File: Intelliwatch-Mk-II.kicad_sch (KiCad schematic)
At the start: 55 parts, among them J1 USB_C_Receptacle_USB2.0_16P, J2 CONN LCD 1.8 TFT SPI, J3 Conn 7S-4D HW-069 I2C, J4 Flashlight Terminals, Q1 NTR2101P, Q2 NDS331N, SW1 EN Switch, SW2 PROG Swtich, SW3 Cherry MX Keyswitch, SW4 Cherry MX Keyswitch, SW5 Cherry MX Keyswitch, SW6 Cherry MX Keyswitch, U1 LM7805, U2 CH340C, U3 SN74HC02N, U4 LM1117T-3.3, U5 74AHC1G04GW_125, U6 74AHC1G04GW_125, U7 ESP32-WROOM-32UE, U8 QMC5883L

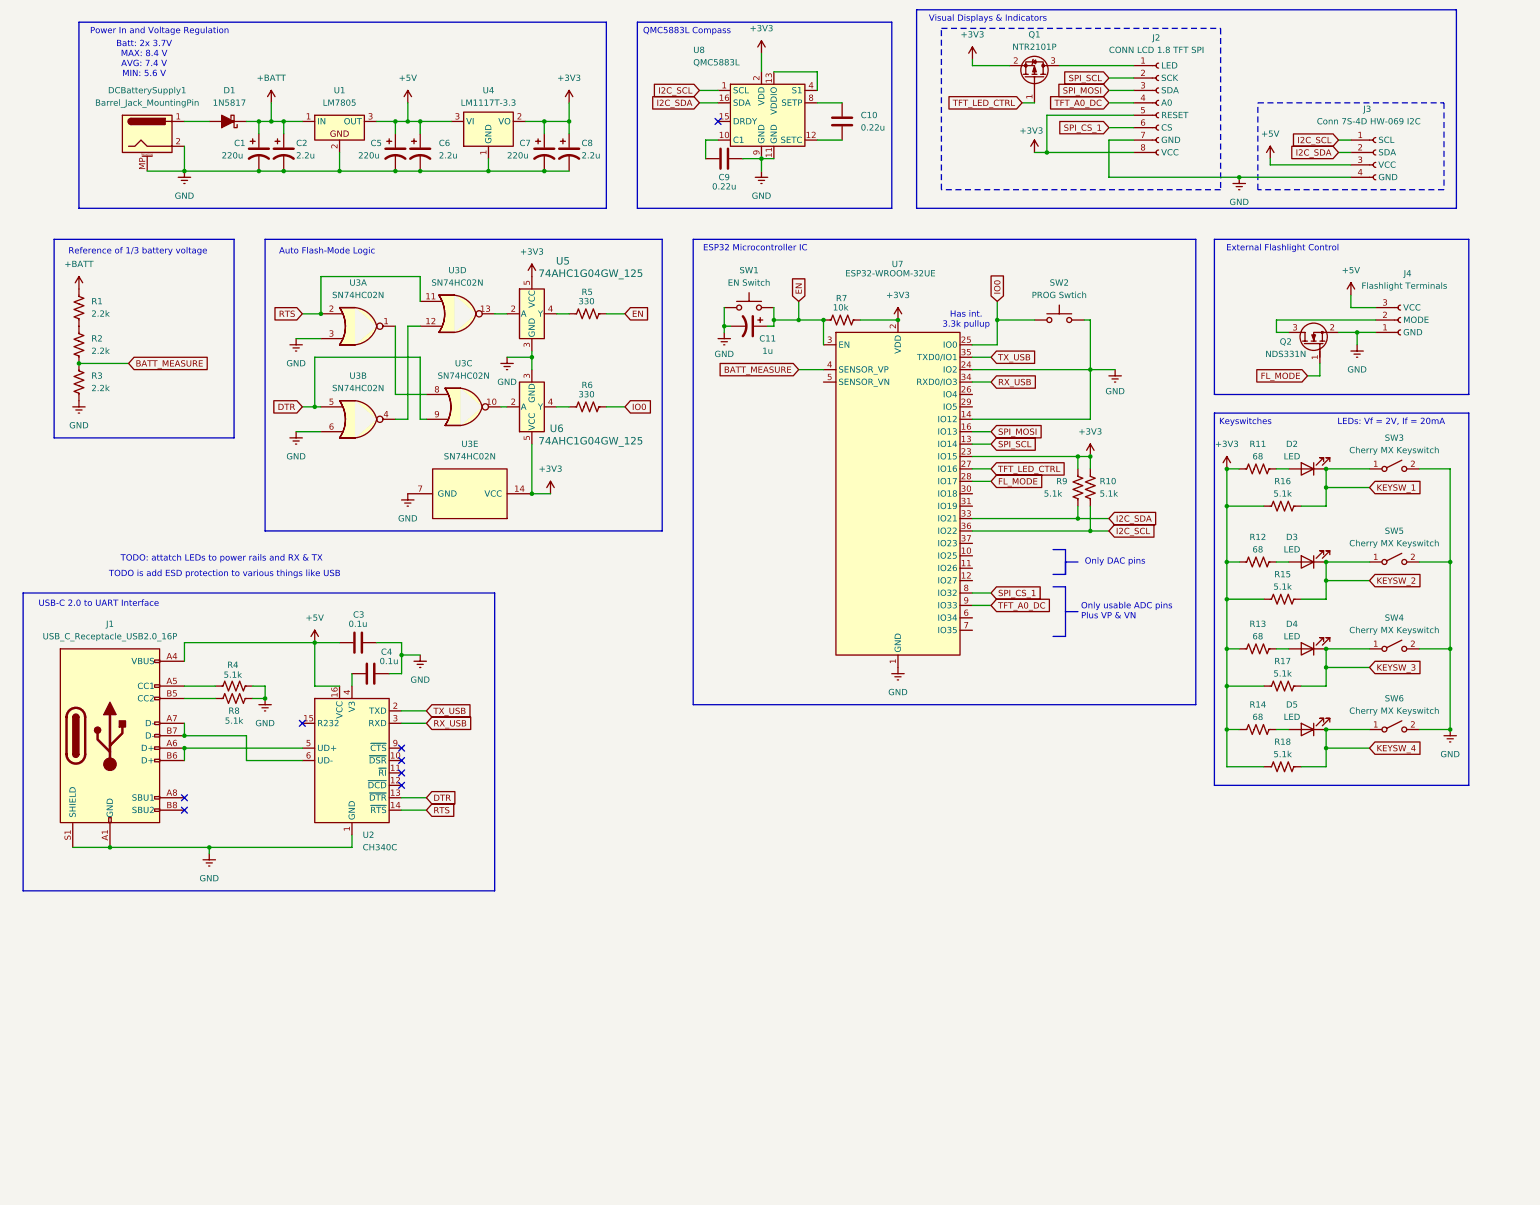
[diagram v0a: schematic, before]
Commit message: ADDED current draw for each component. ADDED flashlight. WIP TODO is sort out whether or not to re-use VSPI MOSI and SCL pins with both LCD and SD card.
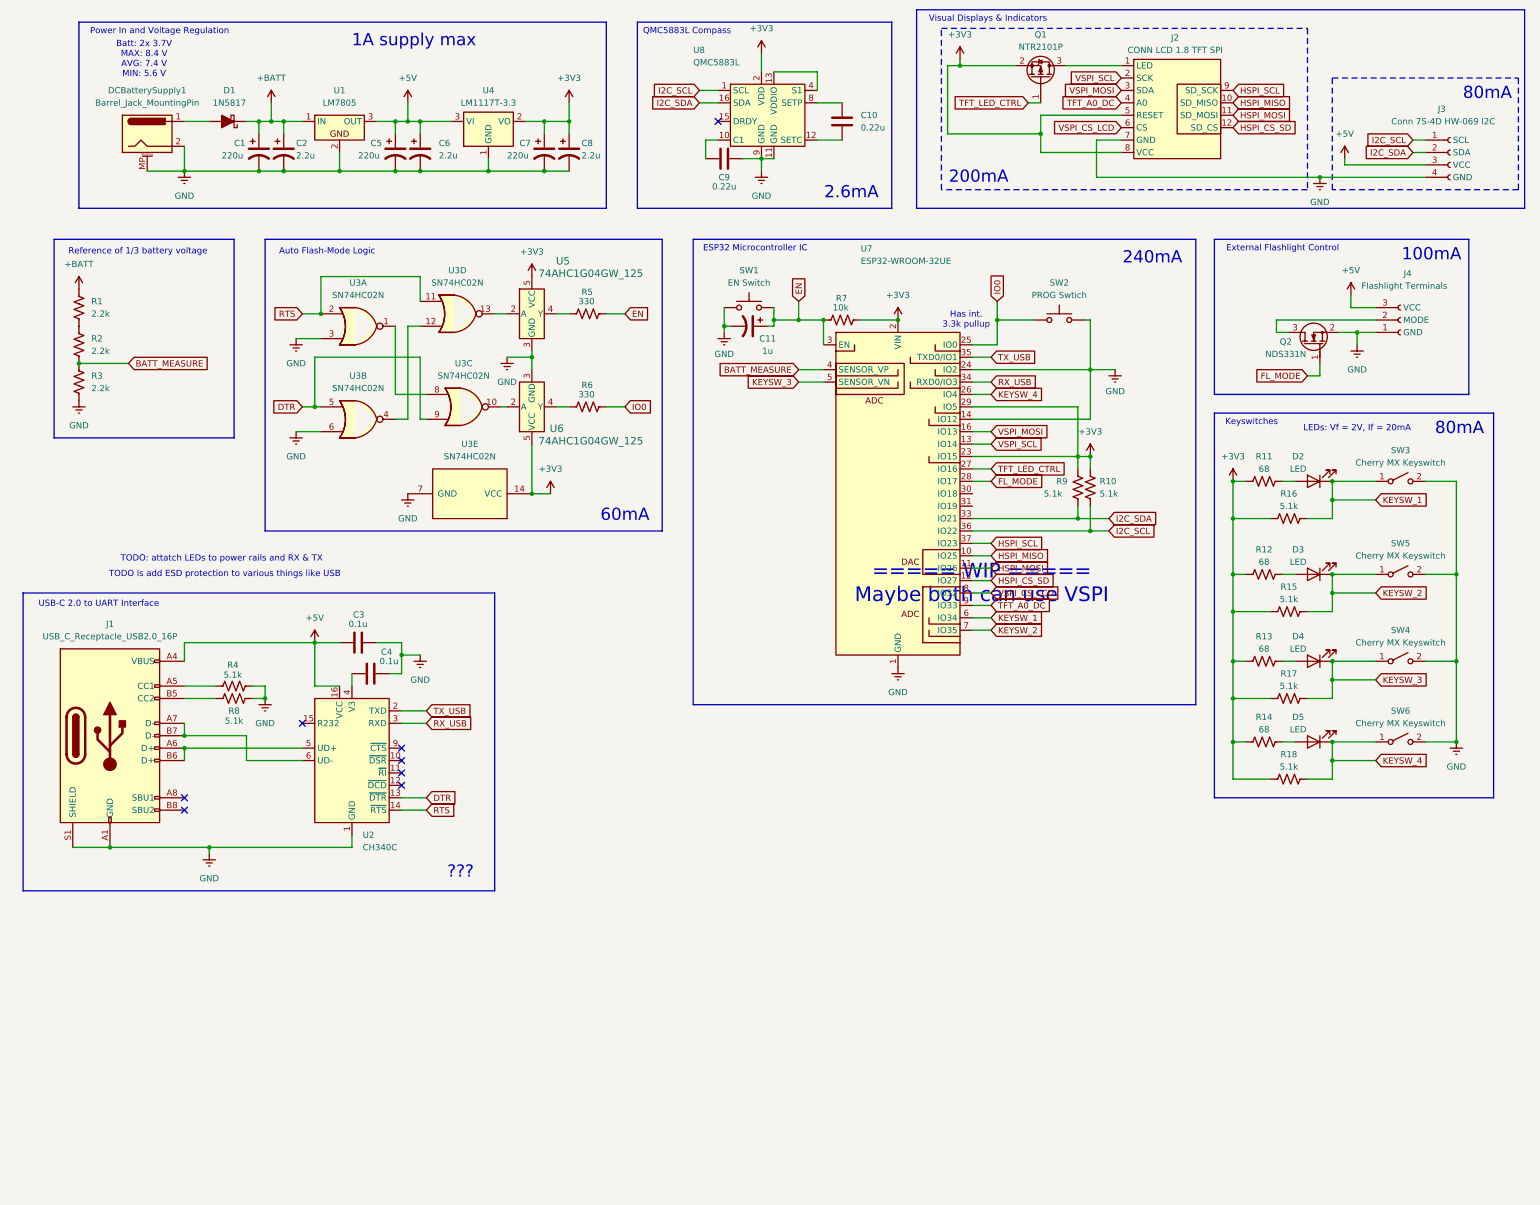
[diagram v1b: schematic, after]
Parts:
- removed U7: ESP32-WROOM-32UE, RF_Module:ESP32-WROOM-32UE, symbol RF_Module:ESP32-WROOM-32UE
- added U7: ESP32-WROOM-32UE, RF_Module:ESP32-WROOM-32UE, symbol ZCustomSymbols:ESP32-WROOM-32UE
- U2: footprint Package_SO:SOIC-16_3.9x9.9mm_P1.27mm -> PCM_Package_SO_AKL:SOP-16_4.55x10.3mm_P1.27mm
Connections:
- net +3V3: now also U7.2 (VIN), U7.23 (IO15), U7.29 (IO5)
- net BATT_MEASURE: now also U7.4 (SENSOR_VP)
- net EN: now also U7.3 (EN)
- net FL_MODE: now also U7.28 (IO17)
- net GND: now also U7.1 (GND), U7.14 (IO12), U7.15 (GND), U7.24 (IO2), U7.38 (GND), U7.39 (GND)
- net I2C_SCL: now also U7.36 (IO22)
- net I2C_SDA: now also U7.33 (IO21)
- net IO0: now also U7.25 (IO0)
- net KEYSW_1: now also U7.6 (IO34)
- net KEYSW_2: now also U7.7 (IO35)
- net KEYSW_3: now also U7.5 (SENSOR_VN)
- net KEYSW_4: now also U7.26 (IO4)
- net RX_USB: now also U7.34 (RXD0/IO3)
- net TFT_A0_DC: now also U7.9 (IO33)
- net TFT_LED_CTRL: now also U7.27 (IO16)
- net TX_USB: now also U7.35 (TXD0/IO1)
- net SPI_CS_1 renamed VSPI_CS_LCD
- net VSPI_CS_LCD: now also U7.8 (IO32)
- net SPI_MOSI renamed VSPI_MOSI
- net VSPI_MOSI: now also U7.16 (IO13)
- net SPI_SCL renamed VSPI_SCL
- net VSPI_SCL: now also U7.13 (IO14)
- new net HSPI_CS_SD: J2.12 (SD_CS), U7.12 (IO27)
- new net HSPI_MISO: J2.10 (SD_MISO), U7.10 (IO25)
- new net HSPI_MOSI: J2.11 (SD_MOSI), U7.11 (IO26)
- new net HSPI_SCL: J2.9 (SD_SCK), U7.37 (IO23)
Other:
- note added: "100mA"
- note added: "1A supply max"
- note added: "2.6mA"
- note added: "200mA"
- note added: "240mA"
- note added: "60mA"
- note added: "80mA"
- note added: "===== WIP ===== Maybe both can use VSPI"
- note added: "???"
- note removed: "Only DAC pins"
- note removed: "Only usable ADC pins Plus VP & VN"
- moved on the sheet: D2, D3, D4, D5, J3, Q1, R11, R12, R13, R14, R15, R16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

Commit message: ADDED ADC for voltmeter/o-scope (NO res-measuring in this one). WIP TODO is determine whether or not SD and LCD will share SPI bus. TODO change voltage regulators to IC-controller buck converters.
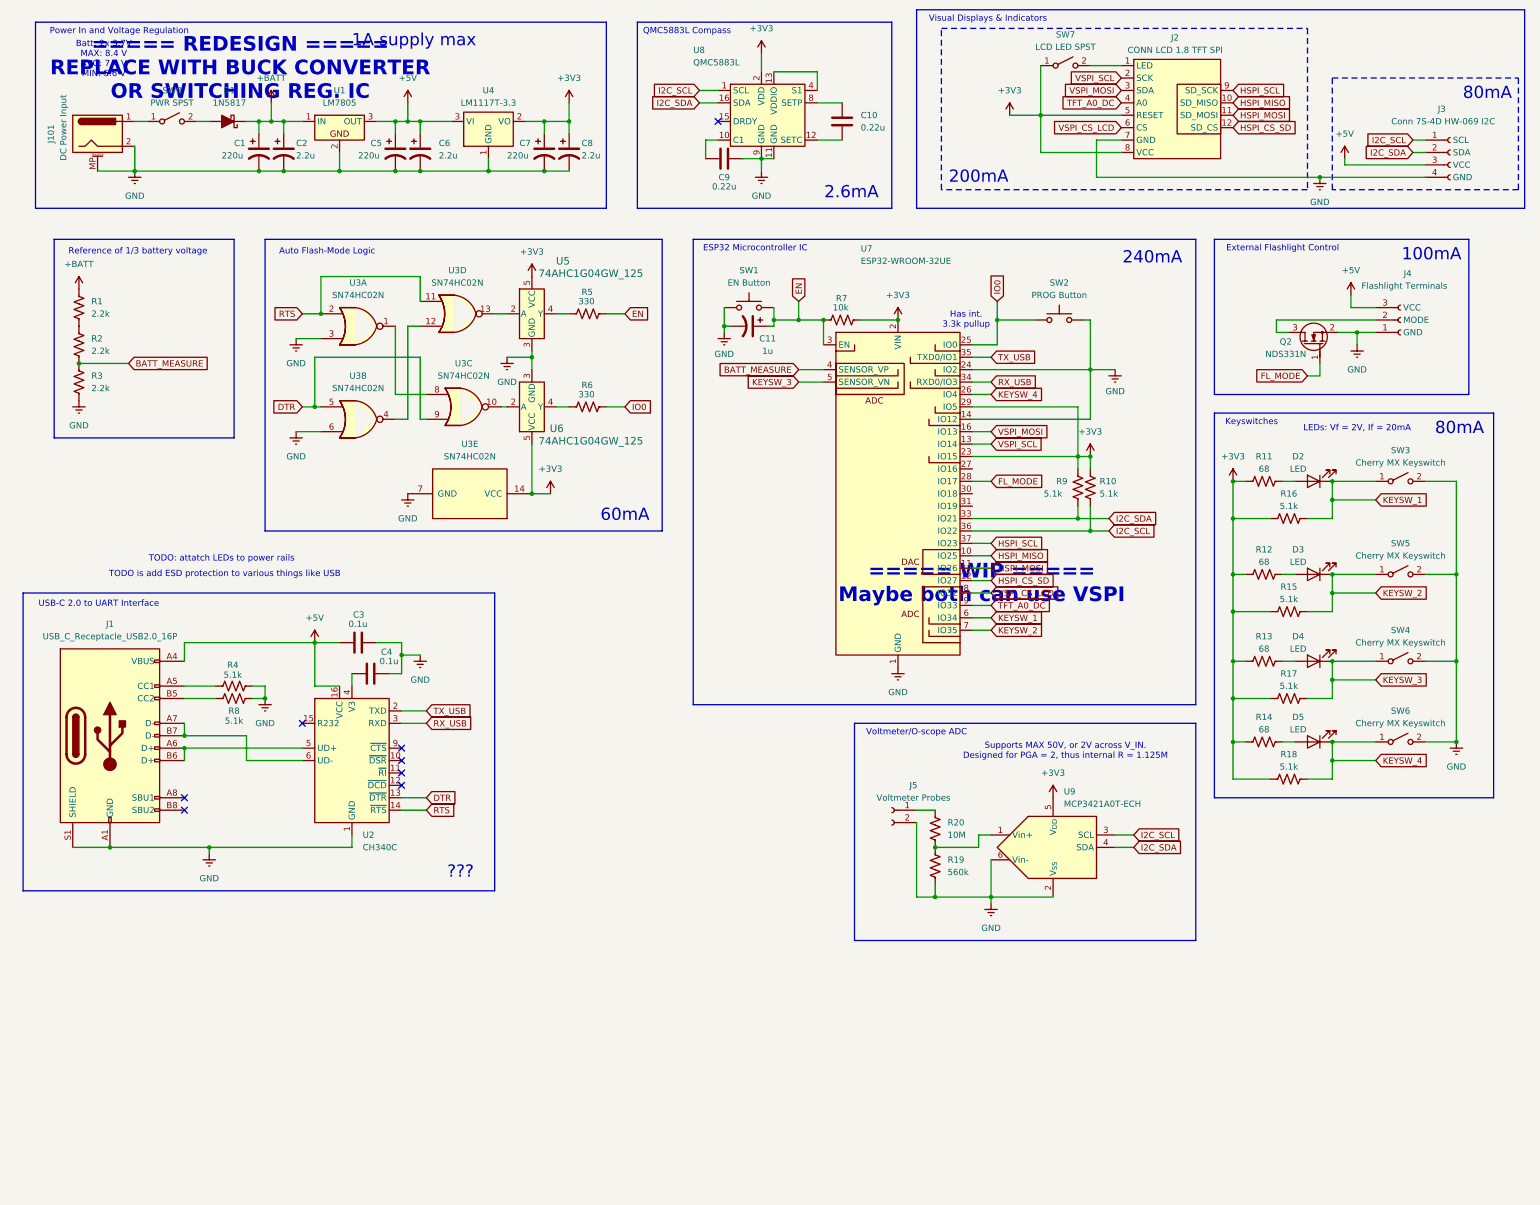
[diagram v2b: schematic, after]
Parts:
- removed Q1: NTR2101P, Package_TO_SOT_SMD:SOT-23, symbol Transistor_FET:NTR2101P
- added J5: Voltmeter Probes, symbol Connector:Conn_01x02_Socket
- added R19: 560k, symbol Device:R_US
- added R20: 10M, symbol Device:R_US
- added SW7: LCD LED SPST, symbol Switch:SW_SPST
- added SW8: PWR SPST, symbol Switch:SW_SPST
- added U9: MCP3421A0T-ECH, PCM_Package_TO_SOT_SMD_AKL:SOT-23-6, symbol Analog_ADC:MCP3421A0T-ECH
- J101: renamed from DCBatterySupply1; value Barrel_Jack_MountingPin -> DC Power Input
- SW1: value EN Switch -> EN Button
- SW2: value PROG Swtich -> PROG Button
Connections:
- net +3V3: now also SW7.1 (A), U9.5 (V_{DD})
- net GND: now also J5.2 (Pin_2), R19.2, U9.2 (V_{SS}), U9.6 (Vin-)
- net I2C_SCL: now also U9.3 (SCL)
- net I2C_SDA: now also U9.4 (SDA)
- net at D1.2 (A): now also SW8.2 (B); no longer J101.1
- net at J2.1 (LED): now also SW7.2 (B)
- net TFT_LED_CTRL: no longer names the net of U7.27 (IO16)
- new net: R19.1, R20.1, U9.1 (Vin+)
- new net: J5.1 (Pin_1), R20.2
- new net: J101.1, SW8.1 (A)
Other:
- note added: "===== REDESIGN ===== REPLACE WITH BUCK CONVERTER OR SWITCHING REG. IC"
- note added: "Supports MAX 50V, or 2V across V_IN. Designed for PGA = 2, thus internal R = 1.125M"
- note added: "TODO: attatch LEDs to power rails"
- note added: "Voltmeter/O-scope ADC"
- note removed: "TODO: attatch LEDs to power rails and RX & TX"
- moved on the sheet: J101

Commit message: ADDED 3.3V step-down switching regulator (buck converter). TODO delete old power setup, but keep 5V regulator because that has low maximum short-term current draw so it's fine.
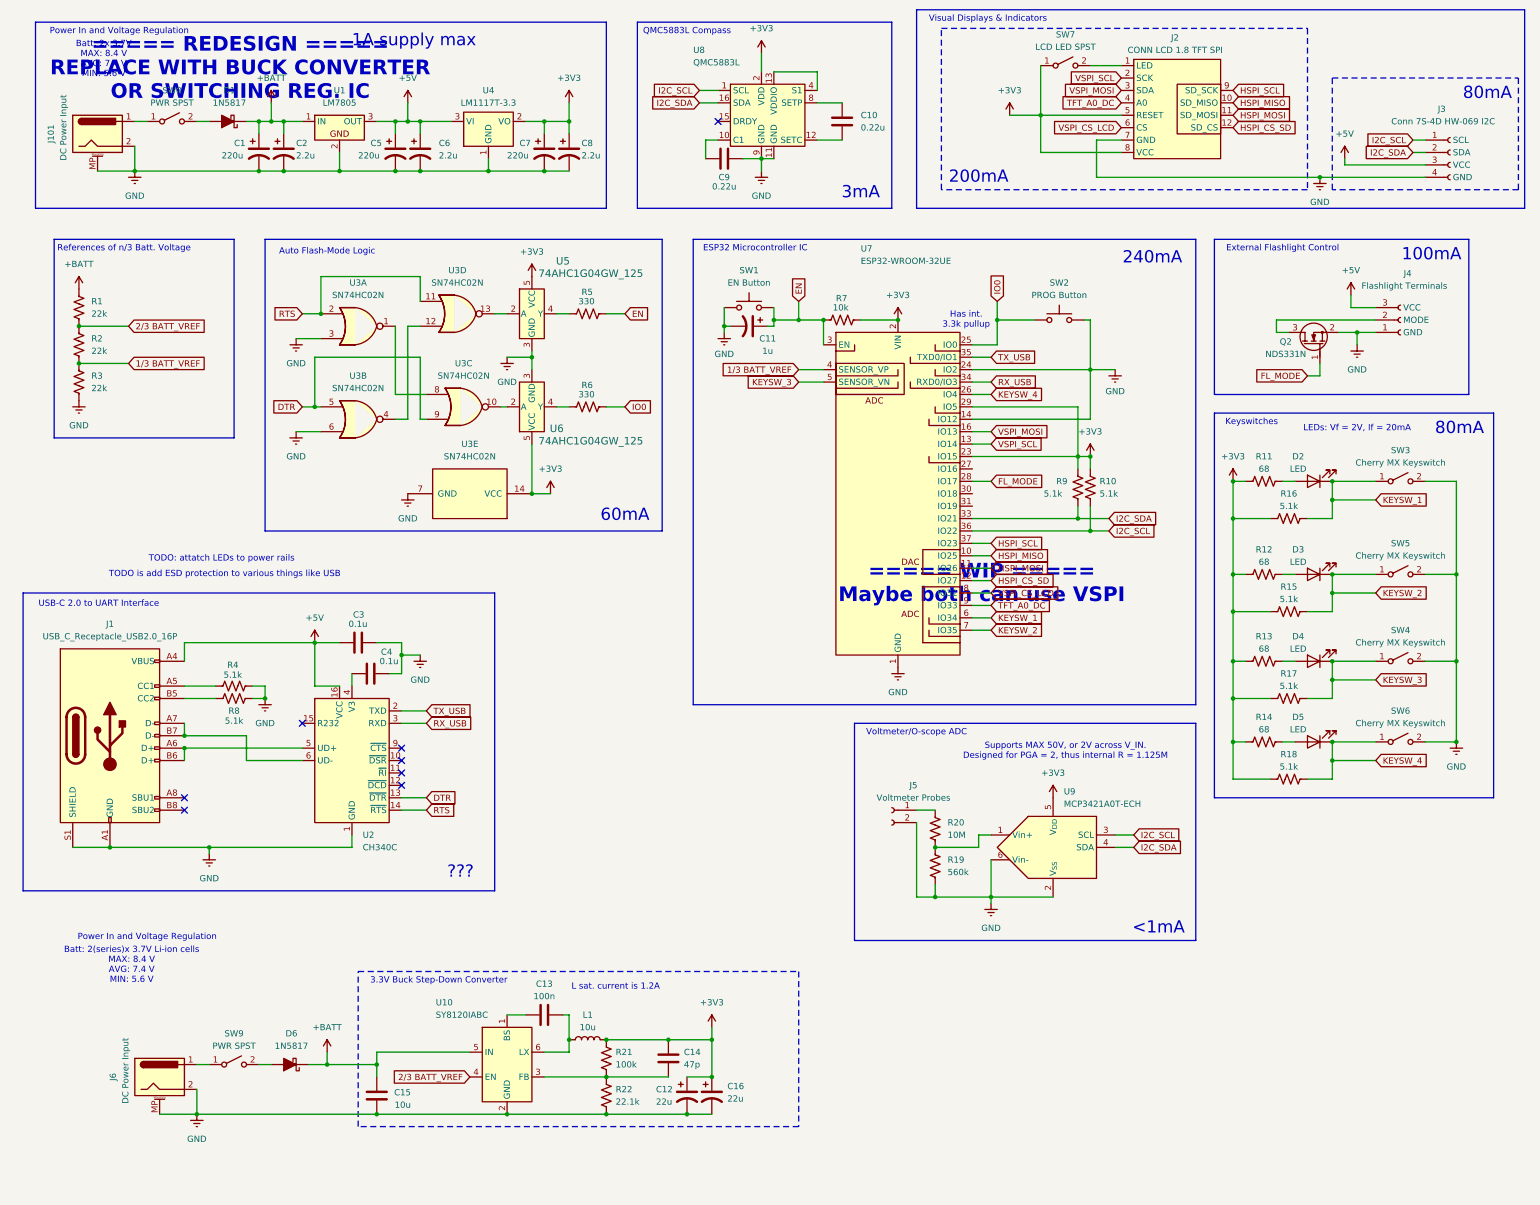
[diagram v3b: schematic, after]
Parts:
- added C12, C16: 22u, symbol Device:C_Polarized_US
- added C13: 100n, symbol Device:C
- added C14: 47p, symbol Device:C
- added C15: 10u, symbol Device:C
- added D6: 1N5817, symbol Device:D_Schottky_Filled
- added J6: DC Power Input, Connector_BarrelJack:BarrelJack_Horizontal, symbol Connector:Barrel_Jack_MountingPin
- added L1: 10u, symbol Device:L
- added R21: 100k, symbol Device:R_US
- added R22: 22.1k, symbol Device:R_US
- added SW9: PWR SPST, symbol Switch:SW_SPST
- added U10: SY8120IABC, Package_TO_SOT_SMD:SOT-23-6, symbol ZCustomSymbols:SY8120IABC
- R1, R2, R3: value 2.2k -> 22k
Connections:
- net +3V3: now also C12.1, C14.1, C16.1, L1.2, R21.1
- net +BATT: now also C15.1, D6.1 (K), U10.5 (IN)
- net GND: now also C12.2, C15.2, C16.2, J6.2, J6.MP (MountPin), R22.2, U10.2 (GND)
- net 2/3 BATT_VREF: now reaches R1.2, R2.1
- net 2/3 BATT_VREF: now also U10.4 (EN)
- net BATT_MEASURE renamed 1/3 BATT_VREF
- new net: J6.1, SW9.1 (A)
- new net: C13.1, U10.1 (BS)
- new net: C14.2, R21.2, R22.1, U10.3 (FB)
- new net: C13.2, L1.1, U10.6 (LX)
- new net: D6.2 (A), SW9.2 (B)
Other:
- note added: "3.3V Buck Step-Down Converter"
- note added: "3mA"
- note added: "<1mA"
- note added: "Batt: 2(series)x 3.7V Li-ion cells MAX: 8.4 V AVG: 7.4 V MIN: 5.6 V"
- note added: "L sat. current is 1.2A"
- note added: "References of n/3 Batt. Voltage"
- note removed: "2.6mA"
- note removed: "Reference of 1/3 battery voltage"
